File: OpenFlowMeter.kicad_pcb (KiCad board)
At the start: 2 copper layers, 55 x 28 mm, 56 parts, among them J1 Screw_Terminal_01x02, J2 Screw_Terminal_01x02, Q1 BC856, Q2 BC856, U1 LT1492, U2 STM32F103C8Tx, U3 LT1492, U4 R-78C3.3-1.0, U6 LT1492

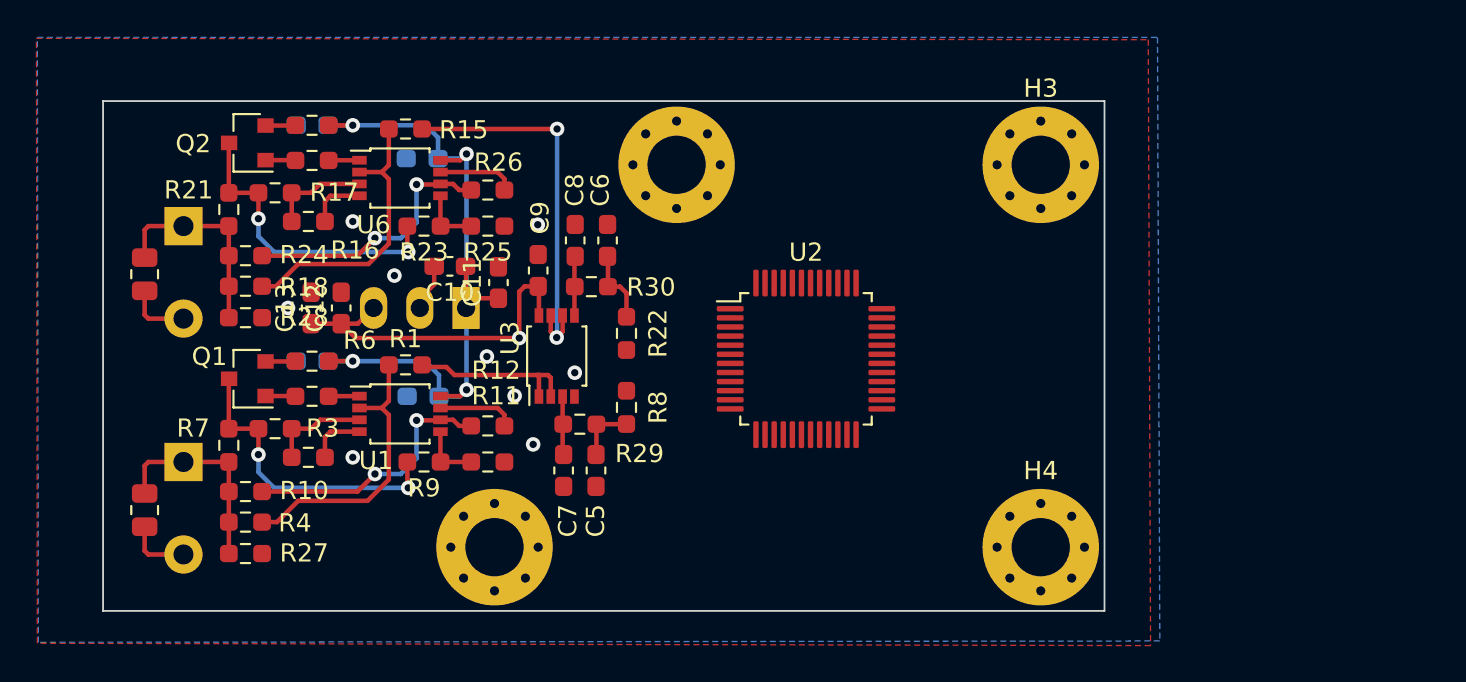
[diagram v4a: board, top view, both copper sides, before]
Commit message: added BUS connector
added box connector (lib from http://smisioto.no-ip.org/elettronica/kicad/kicad-en.htm)
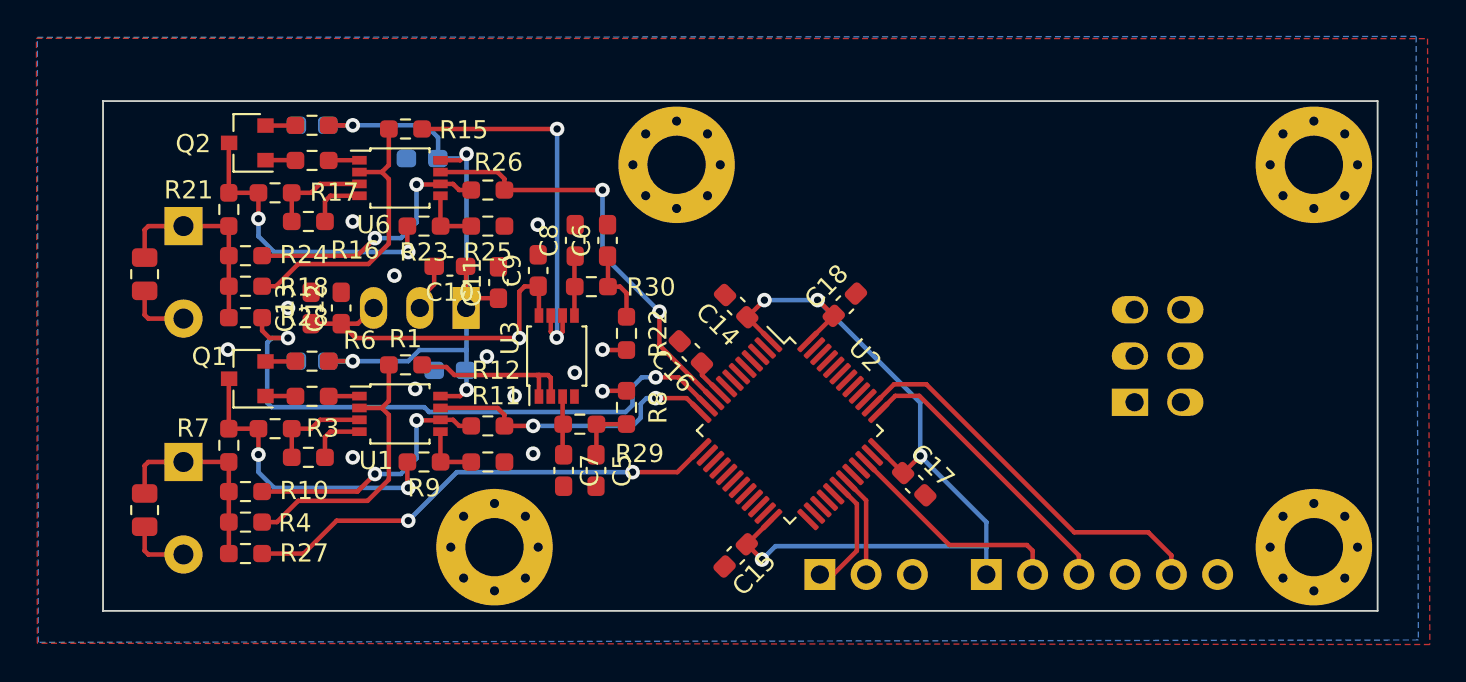
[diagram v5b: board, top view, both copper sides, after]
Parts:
- added C14: C, Capacitor_SMD:C_0603_1608Metric_Pad1.08x0.95mm_HandSolder, F.Cu at (137.9, -13.9)
- added C15: C, Capacitor_SMD:C_0603_1608Metric_Pad1.08x0.95mm_HandSolder, F.Cu at (137.9, -0.25)
- added C16: C, Capacitor_SMD:C_0603_1608Metric_Pad1.08x0.95mm_HandSolder, F.Cu at (135.5, -11.4)
- added C17: C, Capacitor_SMD:C_0603_1608Metric_Pad1.08x0.95mm_HandSolder, F.Cu at (147.7, -4.17)
- added C18: C, Capacitor_SMD:C_0603_1608Metric_Pad1.08x0.95mm_HandSolder, F.Cu at (143.9, -14.0)
- added J3: Conn_01x06, Connector_PinHeader_2.54mm:PinHeader_1x06_P2.54mm_Vertical, B.Cu at (151.7, 0.79)
- added J4: Conn_02x03_Odd_Even, w_conn_strip:vasch_strip_3x2_90, B.Cu at (166.2, -11.2)
- added J5: Conn_01x03, Connector_PinHeader_2.54mm:PinHeader_1x03_P2.54mm_Vertical, B.Cu at (142.5, 0.79)
- added kibuzzard-61D95B1A: G***, kibuzzard-61D95B1A, B.Cu at (154.2, -4.49)
- added kibuzzard-61D95C3F: G***, kibuzzard-61D95C3F, B.Cu at (156.8, -4.62)
- added kibuzzard-61D95C57: G***, kibuzzard-61D95C57, B.Cu at (151.7, -3.45)
- added kibuzzard-61D95C65: G***, kibuzzard-61D95C65, B.Cu at (159.3, -3.56)
- added kibuzzard-61D98FBD: G***, kibuzzard-61D98FBD, B.Cu at (142.5, -3.15)
- added kibuzzard-61D98FCC: G***, kibuzzard-61D98FCC, B.Cu at (145.1, -3.05)
- C1, C2, C3, C4, C5, C6, C7, C8, C9: footprint Capacitor_SMD:C_0603_1608Metric_Pad1.05x0.95mm_HandSolder -> Capacitor_SMD:C_0603_1608Metric_Pad1.08x0.95mm_HandSolder
- moved H3 15.0 mm to (169.7, -21.7)
- moved H4 15.0 mm to (169.7, -0.71)
- moved U2 4.04 mm to (140.9, -7.11), turned to -45 degrees
- moved C2 2.05 mm to (122.2, -10.4)
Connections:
- net /Current Source 1/ISET renamed /ISET 1
- net /Current Source 2/ISET renamed /ISET 2
- R12 pad 1: /Current Source 1/IMEAS -> /I1
- R26 pad 1: /Current Source 2/IMEAS -> /I2
- R27 pad 1: /Current Source 1/UMEAS -> /U1
- R28 pad 1: /Current Source 2/UMEAS -> /U2
- U1 pad 7: /Current Source 1/IMEAS -> /I1
- U2 pad 10: unconnected-(U2-Pad10) -> /I2
- U2 pad 11: unconnected-(U2-Pad11) -> /U2
- U2 pad 12: unconnected-(U2-Pad12) -> /I1
- U2 pad 13: unconnected-(U2-Pad13) -> /U1
- U2 pad 20: unconnected-(U2-Pad20) -> /Controller/TDO
- U2 pad 21: unconnected-(U2-Pad21) -> /Controller/I2C2_SCL
- U2 pad 22: unconnected-(U2-Pad22) -> /Controller/I2C2_SDA
- U2 pad 30: unconnected-(U2-Pad30) -> /Controller/UART1_TX
- U2 pad 31: unconnected-(U2-Pad31) -> /Controller/UART1_RX
- U2 pad 34: unconnected-(U2-Pad34) -> /Controller/TMS_SWDIO
- U2 pad 37: unconnected-(U2-Pad37) -> /Controller/TCK_SWCLK
- U2 pad 38: unconnected-(U2-Pad38) -> /Controller/TDI
- U2 pad 42: unconnected-(U2-Pad42) -> /Controller/I2C1_SCL
- U2 pad 43: unconnected-(U2-Pad43) -> /Controller/I2C1_SDA
- U2 pad 45: unconnected-(U2-Pad45) -> /Controller/CAN_RX
- U2 pad 46: unconnected-(U2-Pad46) -> /Controller/CAN_TX
- U2 pad 5: unconnected-(U2-Pad5) -> /Controller/RCC_OSC_IN
- U2 pad 6: unconnected-(U2-Pad6) -> /Controller/RCC_OSC_OUT
- U6 pad 7: /Current Source 2/IMEAS -> /I2
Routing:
- net +3V3: track 19.5 -> 68.8 mm, vias 1 -> 5
- net /U2: track 0.00 -> 33.3 mm, vias 0 -> 2
- net /U1: track 0.00 -> 26.5 mm, vias 0 -> 2
- net /I2: track 0.00 -> 23.7 mm, vias 0 -> 2
- net /Controller/TDI: track 0.00 -> 21.9 mm
- net /I1: track 0.00 -> 16.5 mm, vias 0 -> 2
- net /Controller/TCK_SWCLK: track 0.00 -> 16.0 mm
- net /Controller/TMS_SWDIO: track 0.00 -> 12.5 mm
- net /Controller/UART1_TX: track 0.00 -> 6.43 mm
- net /Controller/UART1_RX: track 0.00 -> 5.58 mm
- net /Current Source 1/IMEAS: track 4.28 -> 0.00 mm
- net /Current Source 2/IMEAS: track 4.28 -> 0.00 mm
- net /PWM Filter/IN2: track 0.00 -> 1.33 mm, vias 0 -> 1
- net /PWM Filter/IN1: track 0.00 -> 1.33 mm, vias 0 -> 1
- net /Controller/TDO: track 0.00 -> 0.73 mm
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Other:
- board size 55 x 28 mm -> 70 x 28 mm

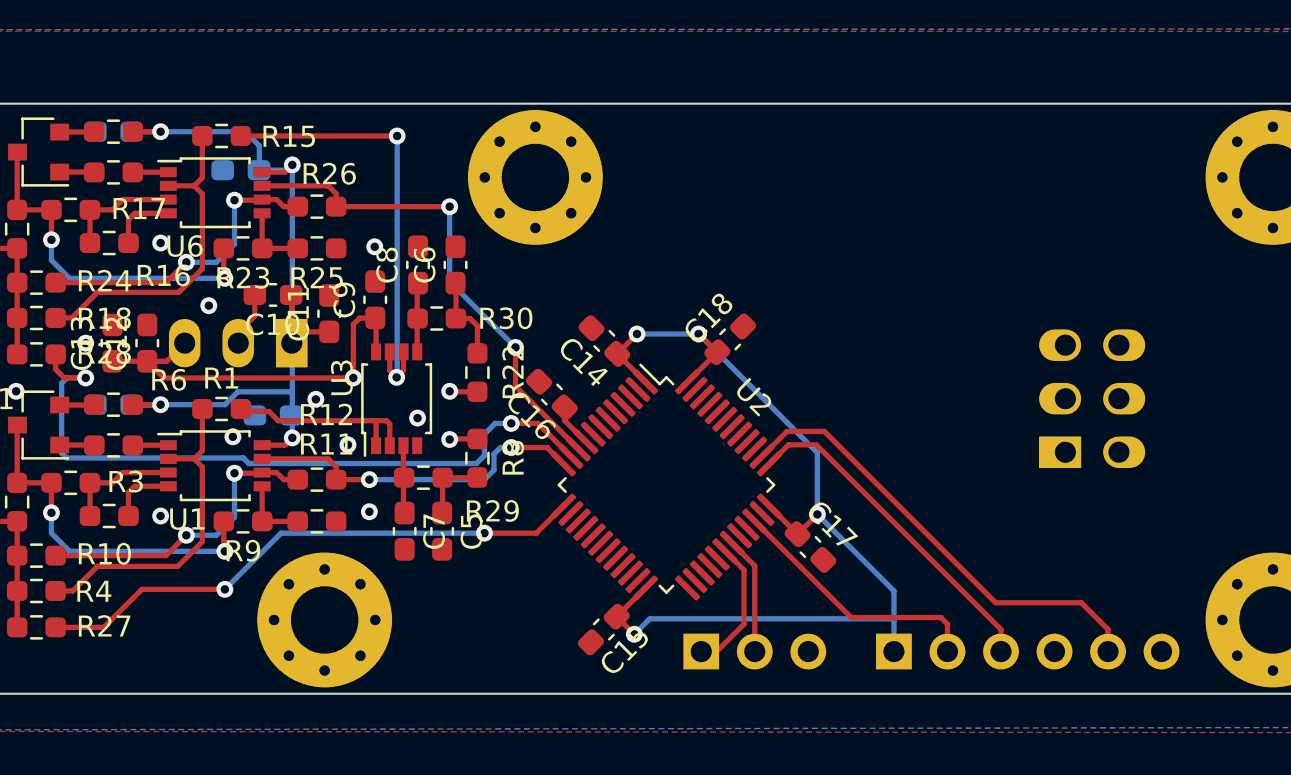
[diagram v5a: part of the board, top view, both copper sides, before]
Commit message: added CAN Transceiver
added SN65HVD231 3.3V CAN Transceiver in order to connect multiple flow meter to a single bus.
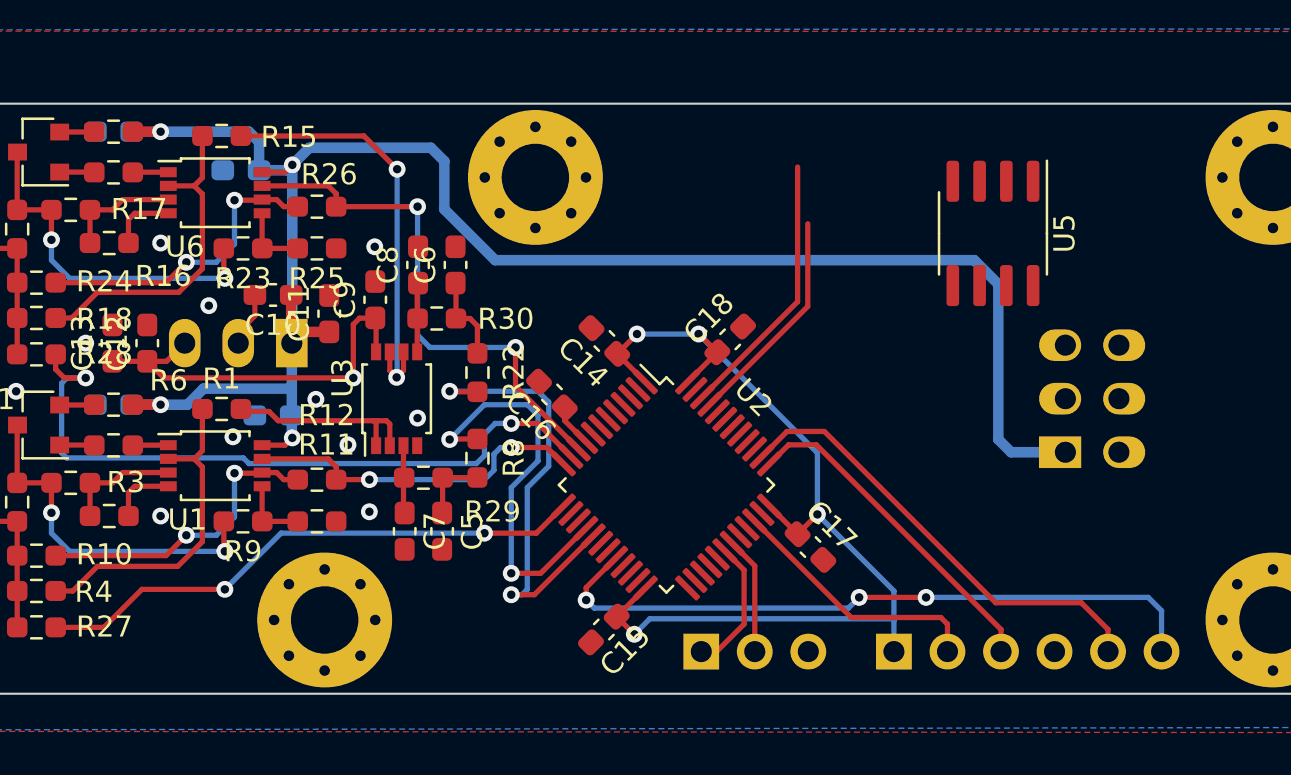
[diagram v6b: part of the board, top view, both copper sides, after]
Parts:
- added U5: SN65HVD231, Package_SO:SOIC-8_3.9x4.9mm_P1.27mm, F.Cu at (156.4, -19.1)
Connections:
- J4 pad 1: unconnected-(J4-Pad1) -> +24V
- J4 pad 3: unconnected-(J4-Pad3) -> /CAN L
- J4 pad 5: unconnected-(J4-Pad5) -> /CAN H
- J4 pad 6: unconnected-(J4-Pad6) -> GND
- R22 pad 2: /PWM Filter/IN2 -> /PWM2
- R8 pad 2: /PWM Filter/IN1 -> /PWM1
- U2 pad 16: unconnected-(U2-Pad16) -> /PWM1
- U2 pad 17: unconnected-(U2-Pad17) -> /PWM2
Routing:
- net +24V: track 41.0 -> 91.1 mm
- net /Controller/TDO: track 0.73 -> 33.2 mm, vias 0 -> 3
- net /PWM2: track 0.00 -> 21.5 mm, vias 0 -> 2
- net /PWM1: track 0.00 -> 18.9 mm, vias 0 -> 2
- net /Controller/CAN_TX: track 0.00 -> 12.8 mm
- net /Controller/CAN_RX: track 0.00 -> 10.5 mm
- net /I2: track 23.7 -> 25.2 mm
- net /PWM Filter/IN2: track 1.33 -> 0.00 mm, vias 1 -> 0
- net /PWM Filter/IN1: track 1.33 -> 0.00 mm, vias 1 -> 0
- net /ISET 2: track 21.5 -> 20.6 mm

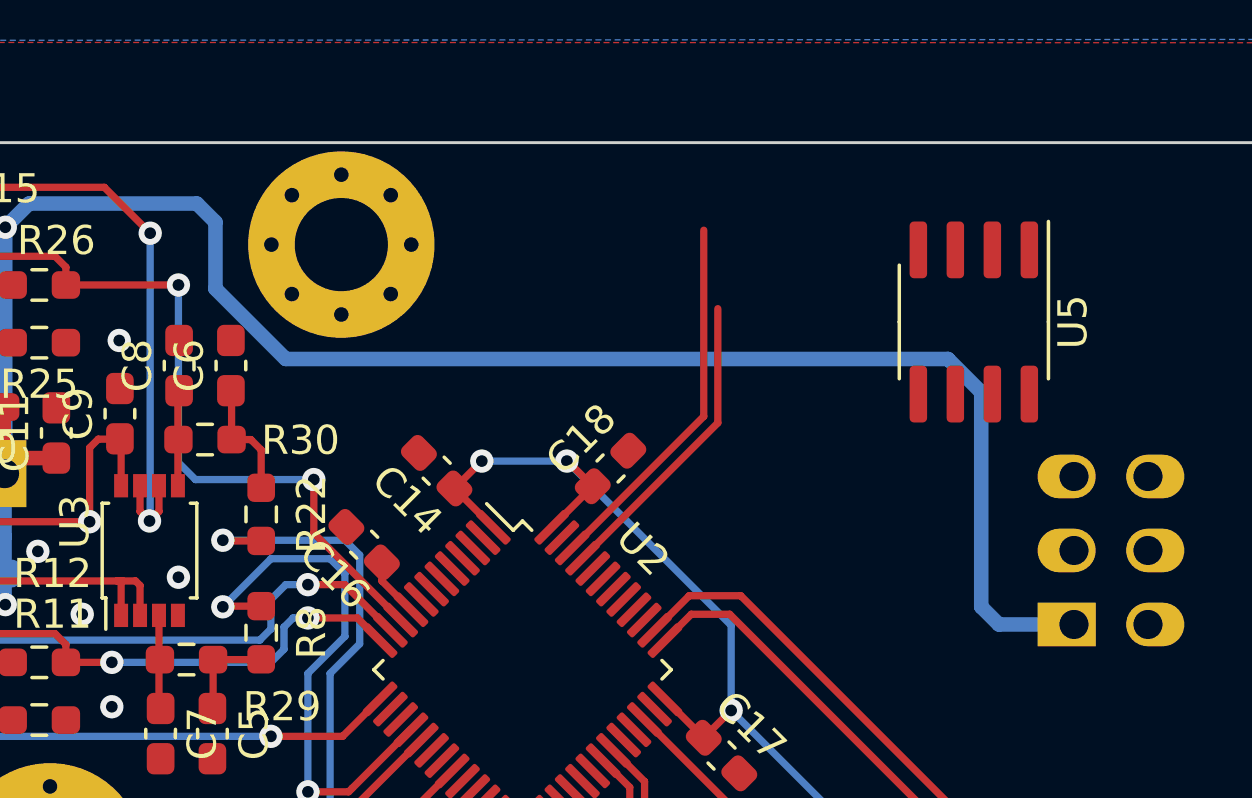
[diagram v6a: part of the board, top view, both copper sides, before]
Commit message: Added crystal for STM32
added 12 MHz MT crystal for STM32's clock input
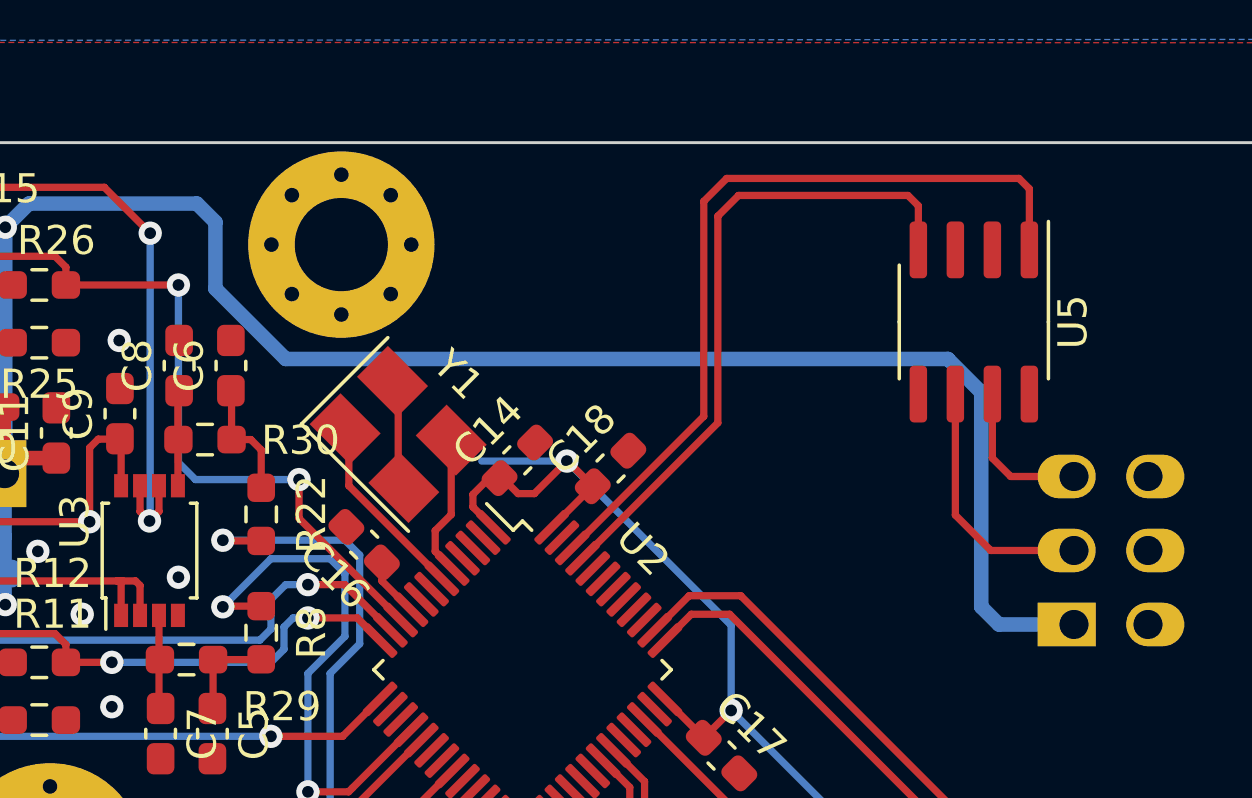
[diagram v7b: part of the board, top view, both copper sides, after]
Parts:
- added Y1: 12 MHz, Crystal:Crystal_SMD_EuroQuartz_MT-4Pin_3.2x2.5mm_HandSoldering, F.Cu at (136.6, -15.2)
- moved C14 2.79 mm to (140.7, -14.3), turned to 45 degrees
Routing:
- net /Controller/CAN_TX: track 12.8 -> 27.5 mm
- net /Controller/CAN_RX: track 10.5 -> 22.5 mm
- net /CAN L: track 0.00 -> 8.73 mm
- net /Controller/RCC_OSC_OUT: track 0.00 -> 6.09 mm
- net /CAN H: track 0.00 -> 5.26 mm
- net /Controller/RCC_OSC_IN: track 0.00 -> 4.88 mm
- net GND: track 16.3 -> 20.1 mm
- net +3V3: track 68.8 -> 71.1 mm, vias 5 -> 4
